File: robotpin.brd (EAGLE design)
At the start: 30.5 x 38.1 mm, 10 parts

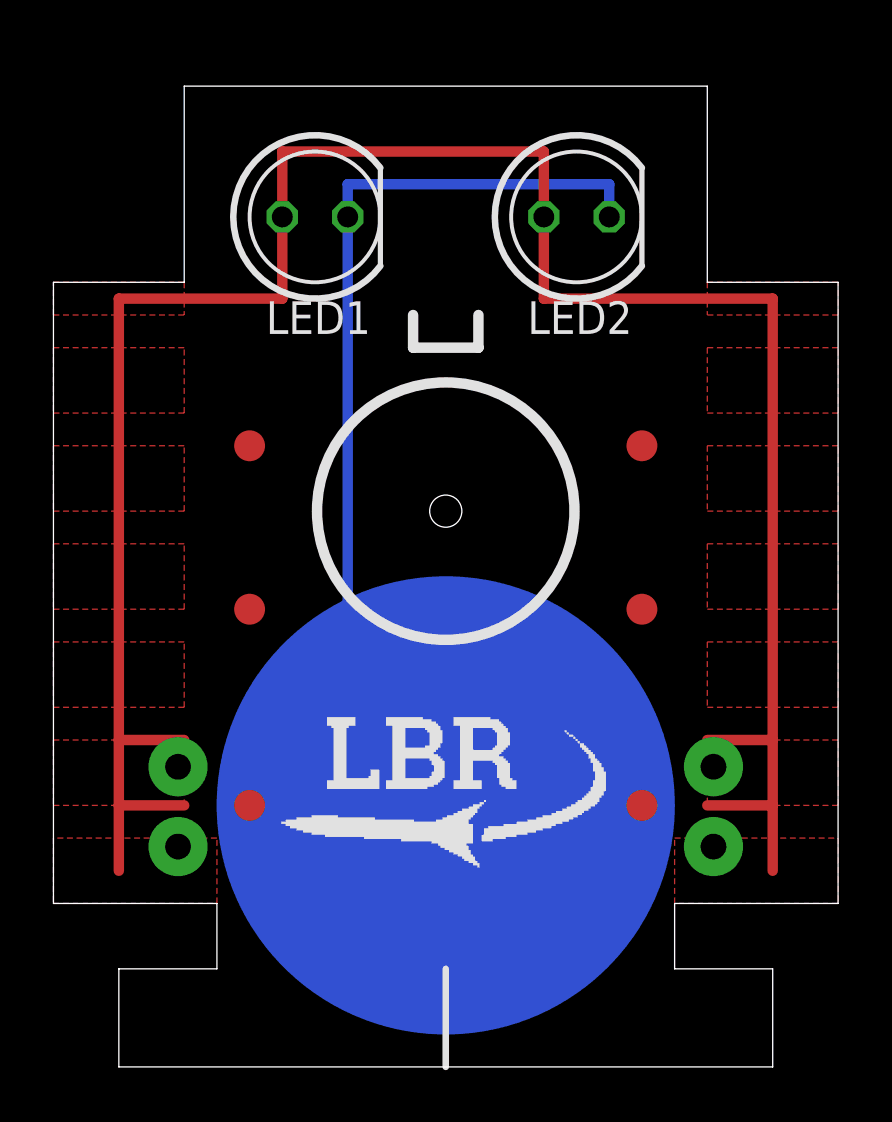
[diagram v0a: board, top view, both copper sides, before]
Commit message: prettify robot pin
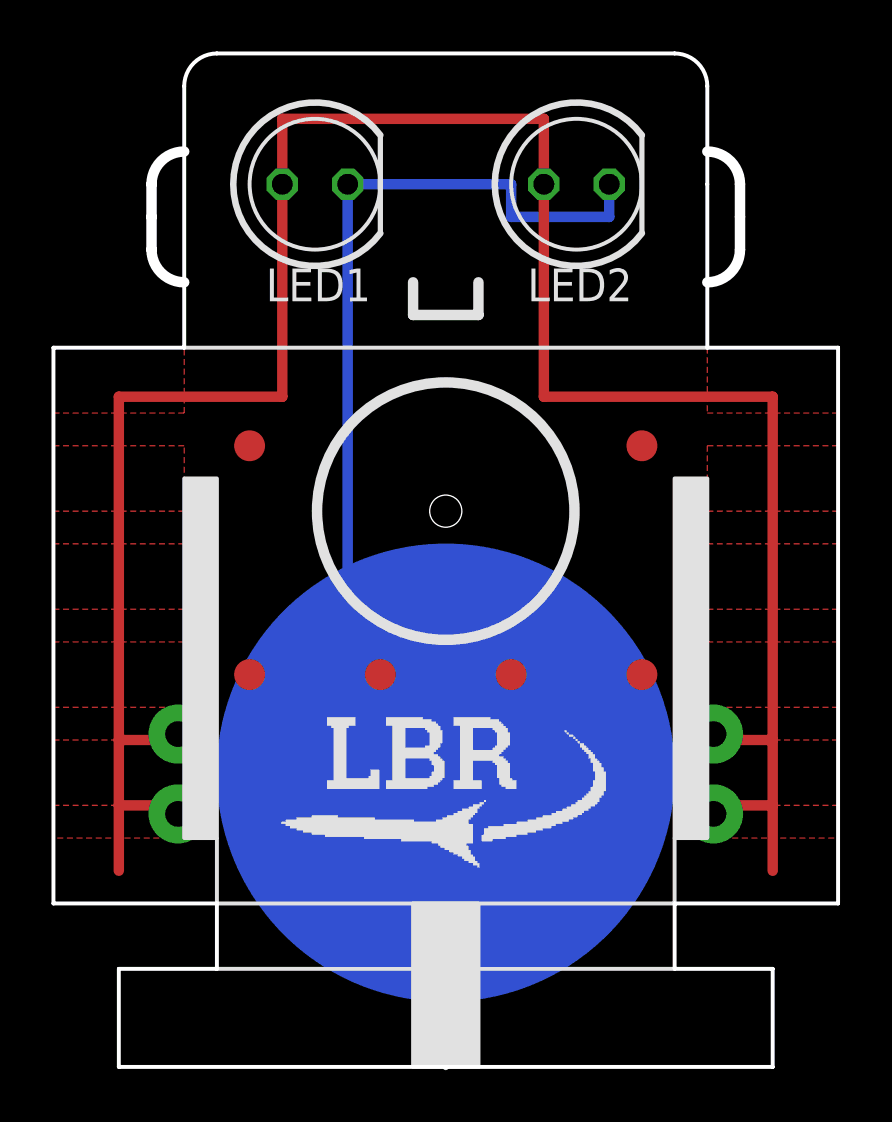
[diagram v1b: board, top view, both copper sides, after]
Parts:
- moved TP3 10.2 mm to (21.6, 24.1)
- moved TP9 10.2 mm to (26.7, 24.1)
- moved TP2 6.35 mm to (16.5, 33.0)
- moved TP8 6.35 mm to (31.8, 33.0)
- moved TP1 5.08 mm to (16.5, 24.1)
- moved TP7 5.08 mm to (31.8, 24.1)
- moved LED1 1.27 mm to (29.2, 43.2)
- moved LED2 1.27 mm to (19.1, 43.2)
- moved U$1 1.27 mm to (24.1, 20.3)
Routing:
- net N$1: track 91.4 -> 94.0 mm
- net N$2: track 38.3 -> 39.4 mm
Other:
- board size 30.5 x 38.1 mm -> 30.5 x 39.4 mm

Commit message: didn't change robot but did?
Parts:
- renumbered U$1 to BATTERY
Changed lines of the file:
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@@
 <attribute name="VALUE" x="22.2504" y="41.3766" size="1.27" layer="27" ratio="10"/>
 </element>
-<element name="U$1" library="battery" package="BAT-HLD-001-THM" value="CR2032-GK" x="24.13" y="20.32" rot="MR0"/>
+<element name="BATTERY" library="battery" package="BAT-HLD-001-THM" value="CR2032-GK" x="24.13" y="20.32" rot="MR0"/>
 <element name="U$2" library="LBR Logo" package="LOGO-0.50&quot;" value="" x="17.78" y="16.51"/>
 <element name="TP1" library="testpad" package="TP12R" value="PTR1TP12R" x="16.51" y="24.13" smashed="yes">
@@
 <signals>
 <signal name="N$1">
-<contactref element="U$1" pad="P$1"/>
-<contactref element="U$1" pad="P$2"/>
-<contactref element="U$1" pad="P$3"/>
-<contactref element="U$1" pad="P$4"/>
+<contactref element="BATTERY" pad="P$1"/>
+<contactref element="BATTERY" pad="P$2"/>
+<contactref element="BATTERY" pad="P$3"/>
+<contactref element="BATTERY" pad="P$4"/>
 <contactref element="LED1" pad="A"/>
 <contactref element="LED2" pad="A"/>
@@
 <signal name="N$2">
 <contactref element="LED1" pad="K"/>
-<contactref element="U$1" pad="P$5"/>
+<contactref element="BATTERY" pad="P$5"/>
 <contactref element="LED2" pad="K"/>
 <wire x1="24.13" y1="20.32" x2="20.32" y2="20.32" width="0.4064" layer="16"/>
